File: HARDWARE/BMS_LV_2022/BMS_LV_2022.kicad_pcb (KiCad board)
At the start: 4 copper layers, 90 x 45 mm, 171 parts, among them J1 Conn_01x06_Male, J11 Conn_01x07_Female, J2 Conn_01x12_Male, J3 USB_B_Mini, J4 Battery+, J5 Battery-, J6 Conn_01x09_Female, Q1 BC846, Q10 BSS138, Q11 SiSS05DN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

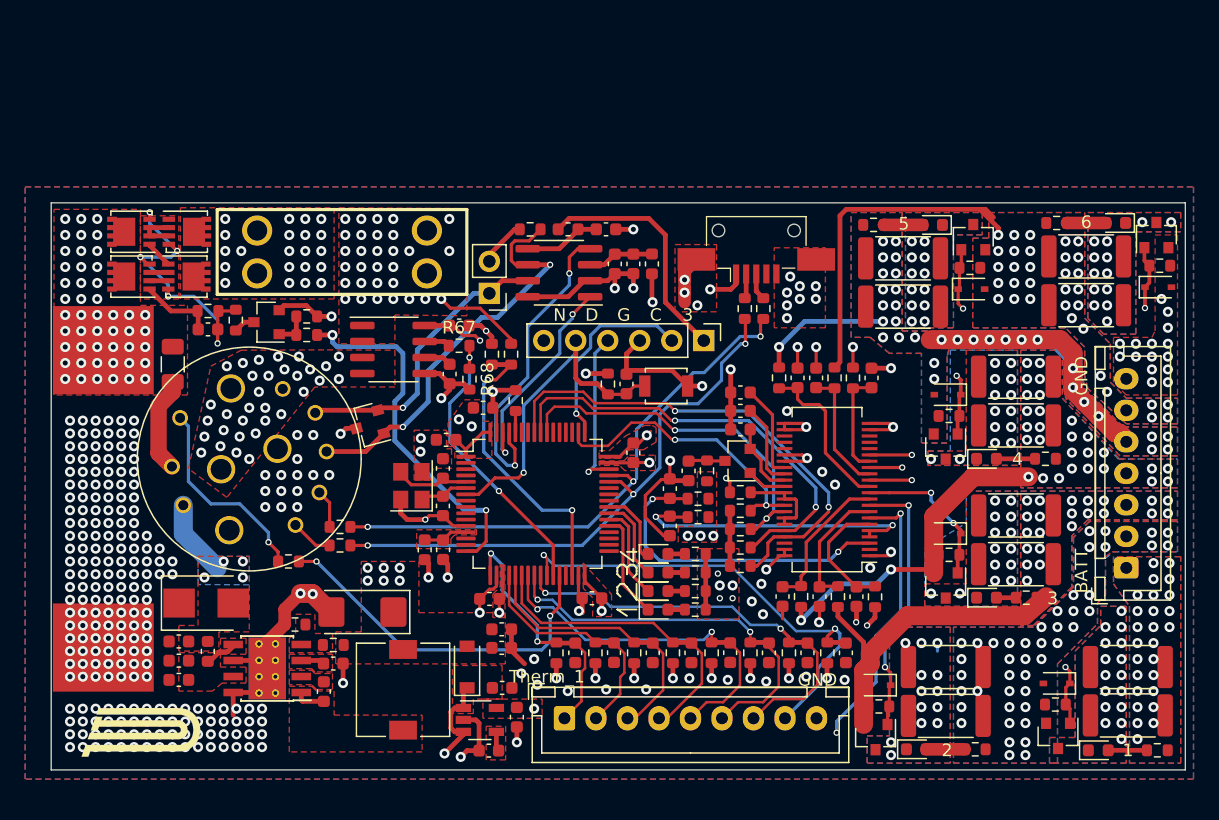
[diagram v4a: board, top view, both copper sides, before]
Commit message: New fuses and programming connector added
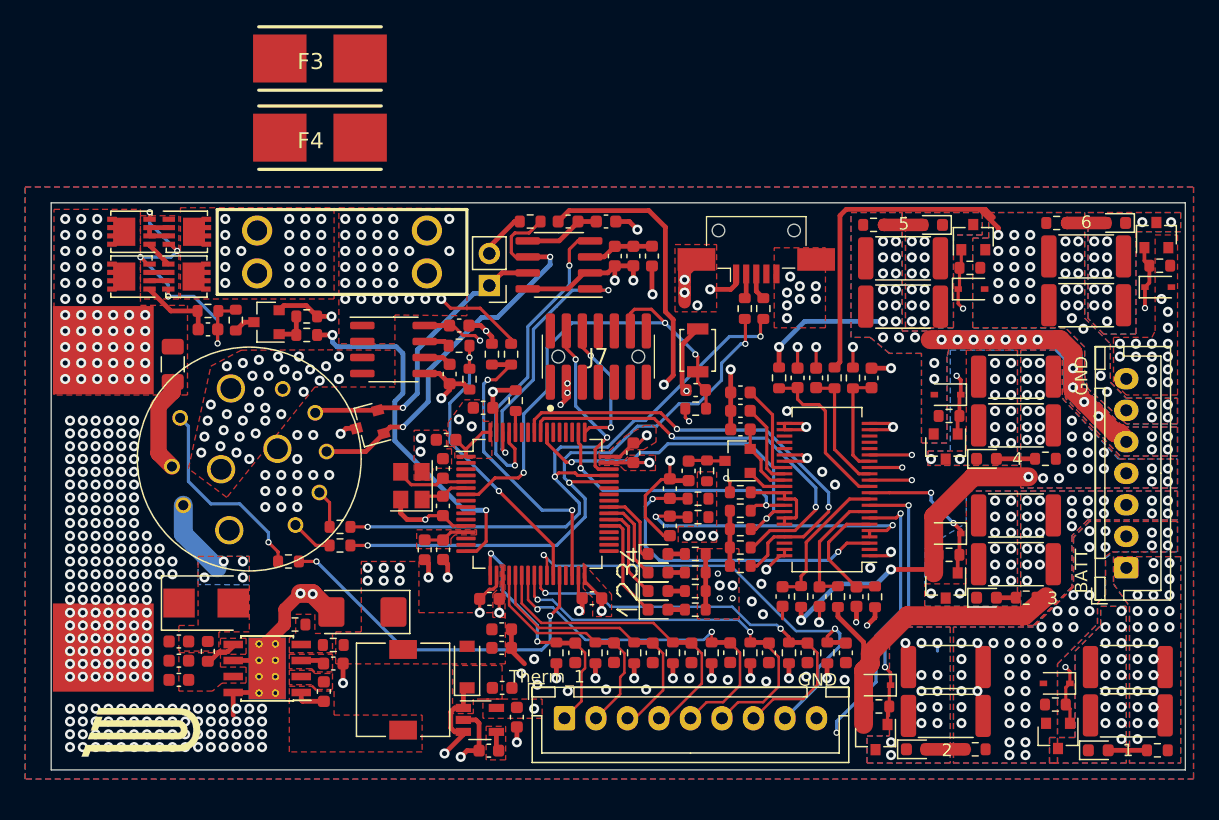
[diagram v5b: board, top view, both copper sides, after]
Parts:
- removed J1: Conn_01x06_Male, Connector_PinHeader_2.54mm:PinHeader_1x06_P2.54mm_Vertical
- added F3: Fuse, footprints:0154001.DRT, F.Cu at (131.3, 68.5)
- added F4: Fuse, footprints:0154001.DRT, F.Cu at (131.3, 74.8)
- added J7: FTSH, footprints:FTSH-107-XX-YYY-DV-K-A, F.Cu at (153.4, 92.2)
- moved R1 7.23 mm to (161.1, 96.3), turned to 180 degrees
- moved C1 5.51 mm to (161.1, 94.9), turned to 0 degrees
- moved SW1 3.78 mm to (161.3, 91.7), turned to 90 degrees
- moved JP2 0.62 mm to (144.8, 86.6)
- moved U4 0.62 mm to (150.3, 84.9)
- moved C7 0.62 mm to (156.2, 84.2)
- moved C8 0.62 mm to (154.7, 84.2)
- moved C9 0.62 mm to (154.0, 81.5)
- moved FB2 0.62 mm to (151.0, 81.5)
- moved FB3 0.62 mm to (157.7, 84.2)
- moved R4 0.62 mm to (148.0, 81.5)
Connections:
- F2 pad 2: Net-(F2-Pad2) -> Net-(Q11-D)
- J2 pad 1: Net-(J2-Pad1) -> unconnected-(J2-Pin_1-Pad1)
- J2 pad 10: /V_Out -> /V_Out_Pin_2
- J2 pad 9: /V_Out -> /V_Out_Pin_1
- J3 pad 4: Net-(J3-Pad4) -> unconnected-(J3-ID-Pad4)
- LTC68101 pad 18: Net-(LTC68101-Pad18) -> unconnected-(LTC68101-GPIO1-Pad18)
- LTC68101 pad 19: Net-(LTC68101-Pad19) -> unconnected-(LTC68101-GPIO2-Pad19)
- LTC68101 pad 2: Net-(LTC68101-Pad2) -> unconnected-(LTC68101-NC-Pad2)
- LTC68101 pad 20: Net-(LTC68101-Pad20) -> unconnected-(LTC68101-GPIO3-Pad20)
- LTC68101 pad 25: Net-(LTC68101-Pad25) -> unconnected-(LTC68101-GPIO4-Pad25)
- LTC68101 pad 26: Net-(LTC68101-Pad26) -> unconnected-(LTC68101-DTEN-Pad26)
- LTC68101 pad 27: Net-(LTC68101-Pad27) -> unconnected-(LTC68101-ISOMD-Pad27)
- LTC68101 pad 42: Net-(LTC68101-Pad42) -> unconnected-(LTC68101-WDT-Pad42)
- Q11 pad 5: Net-(F2-Pad2) -> /CS_IP+
- Q12 pad 5: Net-(F2-Pad2) -> /CS_IP+
- U1 pad 10: Net-(U1-Pad10) -> unconnected-(U1-PC2-Pad10)
- U1 pad 11: Net-(U1-Pad11) -> unconnected-(U1-PC3-Pad11)
- U1 pad 14: Net-(U1-Pad14) -> unconnected-(U1-PA0-Pad14)
- U1 pad 15: Net-(U1-Pad15) -> unconnected-(U1-PA1-Pad15)
- U1 pad 2: Net-(U1-Pad2) -> unconnected-(U1-PC13-Pad2)
- U1 pad 29: Net-(U1-Pad29) -> unconnected-(U1-PB10-Pad29)
- U1 pad 3: Net-(U1-Pad3) -> unconnected-(U1-PC14-OSC32_IN-Pad3)
- U1 pad 33: Net-(U1-Pad33) -> unconnected-(U1-PB12-Pad33)
- U1 pad 34: Net-(U1-Pad34) -> unconnected-(U1-PB13-Pad34)
- U1 pad 35: Net-(U1-Pad35) -> unconnected-(U1-PB14-Pad35)
- U1 pad 36: Net-(U1-Pad36) -> unconnected-(U1-PB15-Pad36)
- U1 pad 4: Net-(U1-Pad4) -> unconnected-(U1-PC15-OSC32_OUT-Pad4)
- U1 pad 41: Net-(U1-Pad41) -> unconnected-(U1-PA8-Pad41)
- U1 pad 42: Net-(U1-Pad42) -> unconnected-(U1-PA9-Pad42)
- U1 pad 43: Net-(U1-Pad43) -> unconnected-(U1-PA10-Pad43)
- U1 pad 51: Net-(U1-Pad51) -> unconnected-(U1-PC10-Pad51)
- U1 pad 52: Net-(U1-Pad52) -> unconnected-(U1-PC11-Pad52)
- U1 pad 53: Net-(U1-Pad53) -> unconnected-(U1-PC12-Pad53)
- U1 pad 54: Net-(U1-Pad54) -> unconnected-(U1-PD2-Pad54)
- U1 pad 58: Net-(U1-Pad58) -> unconnected-(U1-PB6-Pad58)
- U1 pad 59: Net-(U1-Pad59) -> unconnected-(U1-PB7-Pad59)
- U1 pad 8: Net-(U1-Pad8) -> unconnected-(U1-PC0-Pad8)
- U1 pad 9: Net-(U1-Pad9) -> unconnected-(U1-PC1-Pad9)
- U5 pad 3: /V_Out -> Net-(F3-Pad1)
- U5 pad 4: /V_Out -> Net-(F3-Pad1)
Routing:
- net /NRST: track 26.8 -> 39.0 mm, vias 1 -> 3
- net /USB-DP: track 44.7 -> 50.4 mm
- net /SW-CLK: track 15.7 -> 10.8 mm, vias 1 -> 2
- net +3V3: track 56.3 -> 60.6 mm, vias 21 -> 25
- net /CAN-TX: track 17.1 -> 21.3 mm
- net /USB-DM: track 45.6 -> 49.0 mm
- net GND: track 134.2 -> 131.1 mm
- net /MOSI: track 39.5 -> 37.3 mm
- net /MISO: track 35.3 -> 33.2 mm
- net /SW-DIO: track 12.8 -> 13.7 mm, vias 1 -> 2
- net /SCK: track 29.2 -> 28.4 mm
- net /CS: track 22.9 -> 22.1 mm
- net /CAN-RX: track 24.7 -> 25.3 mm
- net /CANL: track 32.6 -> 33.2 mm
- net Net-(F3-Pad1): vias 0 -> 32
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- added copper zone on In1.Cu, net /V_Out_Pin_2
- added copper zone on F.Cu, net Net-(F3-Pad1)
- removed copper zone on F.Cu, net /V_Out
- removed copper zone on In1.Cu, net /V_Out
- removed copper zone on F.Cu, net Net-(F2-Pad2)
- removed copper zone on In1.Cu, net Net-(F2-Pad2)
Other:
- board text removed: "C"
- board text removed: "D"
- board text removed: "G"
- board text removed: "N"

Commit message: Significant changes
-main connector changed to the other side of the pcb because of using socket connector in the new version
-changed usb mini to usb-c
-changed fuse to 2 fuses protecting current path pins separately
-some minor changes in layout
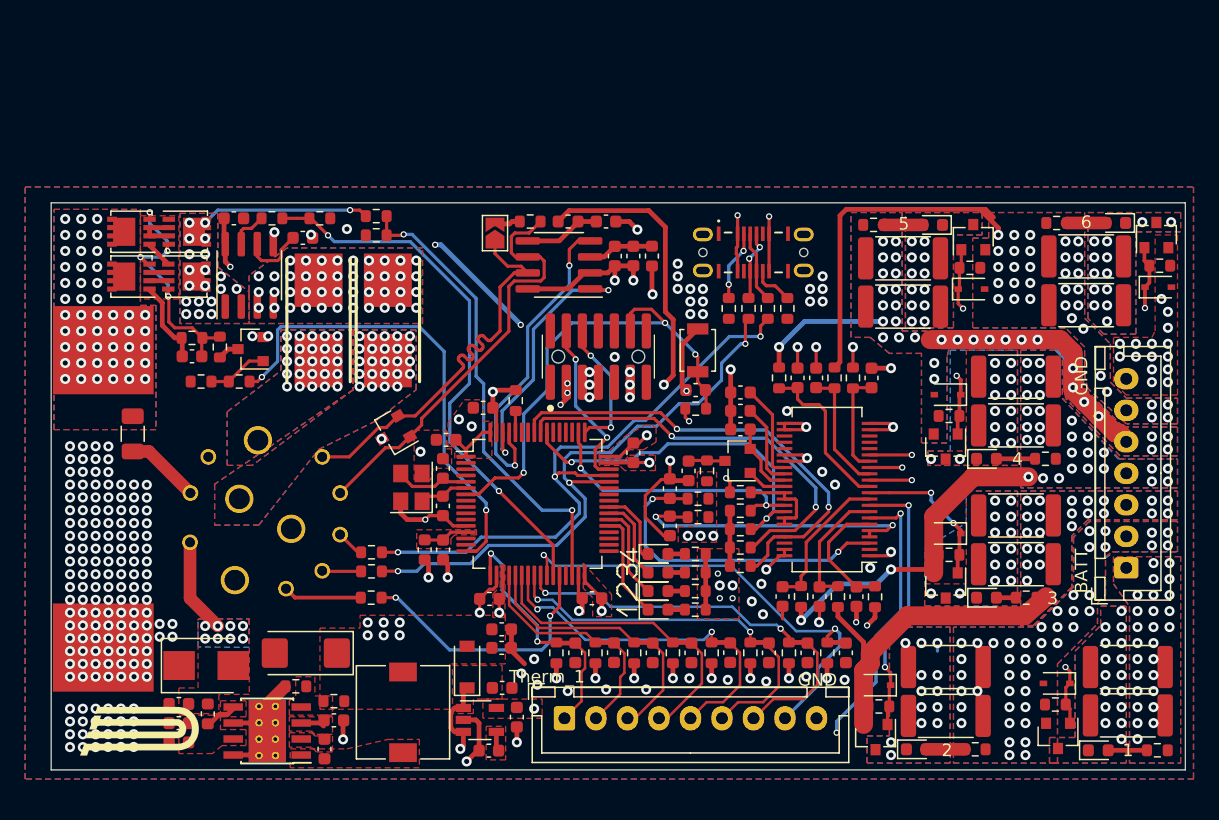
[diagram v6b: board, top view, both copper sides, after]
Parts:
- removed F2: Fuse, footprints:3557-2
- removed J3: USB_B_Mini, Connector_USB:USB_Mini-B_AdamTech_MUSB-B5-S-VT-TSMT-1_SMD_Vertical
- added J1: USB-C_GCT_USB4145-03-0070-C, footprints:USB-C_Receptacle_GCT_USB4145-03-0070-C, F.Cu at (165.7, 83.8)
- added R69: 5.1k, Resistor_SMD:R_0603_1608Metric, F.Cu at (163.8, 88.4)
- added R70: 5.1k, Resistor_SMD:R_0603_1608Metric, F.Cu at (168.4, 88.4)
- J2: moved to B.Cu
- JP2: footprint Connector_PinHeader_2.54mm:PinHeader_1x02_P2.54mm_Vertical -> Jumper:SolderJumper-2_P1.3mm_Open_TrianglePad1.0x1.5mm
- R66: value 2,7k -> 2.7k
- moved F3 21.5 mm to (136.7, 89.3), turned to -90 degrees
- moved C43 19.8 mm to (124.5, 81.2)
- moved R67 18.0 mm to (127.5, 81.2)
- moved R68 17.4 mm to (131.3, 81.2), turned to 0 degrees
- moved C42 15.9 mm to (130.0, 82.8), turned to 0 degrees
- moved R65 15.3 mm to (135.8, 81.1), turned to 0 degrees
- moved F4 14.5 mm to (131.2, 89.3), turned to -90 degrees
- moved R66 13.2 mm to (135.8, 82.6), turned to 180 degrees
- moved U5 12.9 mm to (125.7, 85.8), turned to 90 degrees
- moved R60 9.85 mm to (121.9, 94.2), turned to 180 degrees
- moved R15 7.16 mm to (135.4, 111.3)
- moved R59 6.51 mm to (124.9, 94.2)
- moved F1 6.37 mm to (116.5, 98.3)
- moved C38 5.55 mm to (130.2, 115.7)
- moved C32 4.96 mm to (120.1, 121.3)
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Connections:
- D2 pad 1: /CANL -> /CAN-
- D2 pad 2: /CANH -> /CAN+
- J2 pad 1: unconnected-(J2-Pin_1-Pad1) -> Net-(J2-Pin_1)
- J2 pad 10: /V_Out_Pin_2 -> /V_Out_Pin_1
- J2 pad 12: GND -> /V_Out_Pin_2
- J2 pad 2: /CANH -> Net-(J2-Pin_2)
- J2 pad 3: /CANL -> Net-(J2-Pin_3)
- J2 pad 4: Net-(J2-Pin_4) -> /CAN-
- J2 pad 5: Net-(J2-Pin_5) -> /CAN+
- J2 pad 6: VCC -> unconnected-(J2-Pin_6-Pad6)
- J2 pad 8: Net-(J2-Pin_8) -> VCC
- J2 pad 9: /V_Out_Pin_1 -> GND
- JP2 pad 1: /CANH -> /CAN+
- R13 pad 2: Net-(J2-Pin_4) -> Net-(J2-Pin_3)
- R14 pad 1: Net-(J2-Pin_5) -> Net-(J2-Pin_2)
- R15 pad 1: Net-(J2-Pin_8) -> Net-(J2-Pin_1)
- R4 pad 2: /CANL -> /CAN-
- R8 pad 1: Net-(J3-D+) -> /D+
- R9 pad 2: Net-(J3-D-) -> /D-
- U4 pad 6: /CANL -> /CAN-
- U4 pad 7: /CANH -> /CAN+
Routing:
- net /CAN-: track 0.00 -> 34.0 mm
- net /CANL: track 33.2 -> 0.00 mm, vias 2 -> 0
- net /CAN+: track 0.00 -> 32.4 mm
- net +5V: track 45.7 -> 71.7 mm, vias 8 -> 10
- net GND: track 131.1 -> 105.3 mm, vias 300 -> 240
- net /CANH: track 23.2 -> 0.00 mm, vias 1 -> 0
- net /CurrentSensor_Out: track 23.2 -> 43.4 mm
- net Net-(J2-Pin_8): track 15.9 -> 0.00 mm, vias 1 -> 0
- net /VoltageFuseMeasure: track 23.8 -> 37.3 mm
- net /Switch_Signal: track 28.9 -> 37.9 mm
- net /Interlock: track 28.7 -> 20.9 mm
- net Net-(J2-Pin_1): track 0.00 -> 6.22 mm
- net /CS_IP+: track 7.23 -> 13.4 mm, vias 51 -> 20
- net /D-: track 0.00 -> 5.80 mm, vias 0 -> 2
- net /D+: track 0.00 -> 5.74 mm
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- added copper zone on B.Cu, net +24V
- added copper zone on In2.Cu, net +24V
- added copper zone on B.Cu, net /CS_IP+
- added copper zone on In2.Cu, net /CS_IP+
- added copper zone on B.Cu, net /V_Out_Pin_1
- added copper zone on F.Cu, net /V_Out_Pin_1
- added copper zone on In1.Cu, net /V_Out_Pin_1
- added copper zone on In2.Cu, net /V_Out_Pin_1
- added copper zone on B.Cu, net /V_Out_Pin_2
- added copper zone on F.Cu, net /V_Out_Pin_2
- added copper zone on In2.Cu, net /V_Out_Pin_2
- added copper zone on B.Cu, net Net-(F3-Pad1)
- added copper zone on In1.Cu, net Net-(F3-Pad1)
- added copper zone on In2.Cu, net Net-(F3-Pad1)
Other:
- board text added: "2024"
- board text added: "V2.0"
- board text removed: "2022"
- board text removed: "V1.0"

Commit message: Version 2.0
Grounding corrected and production files added
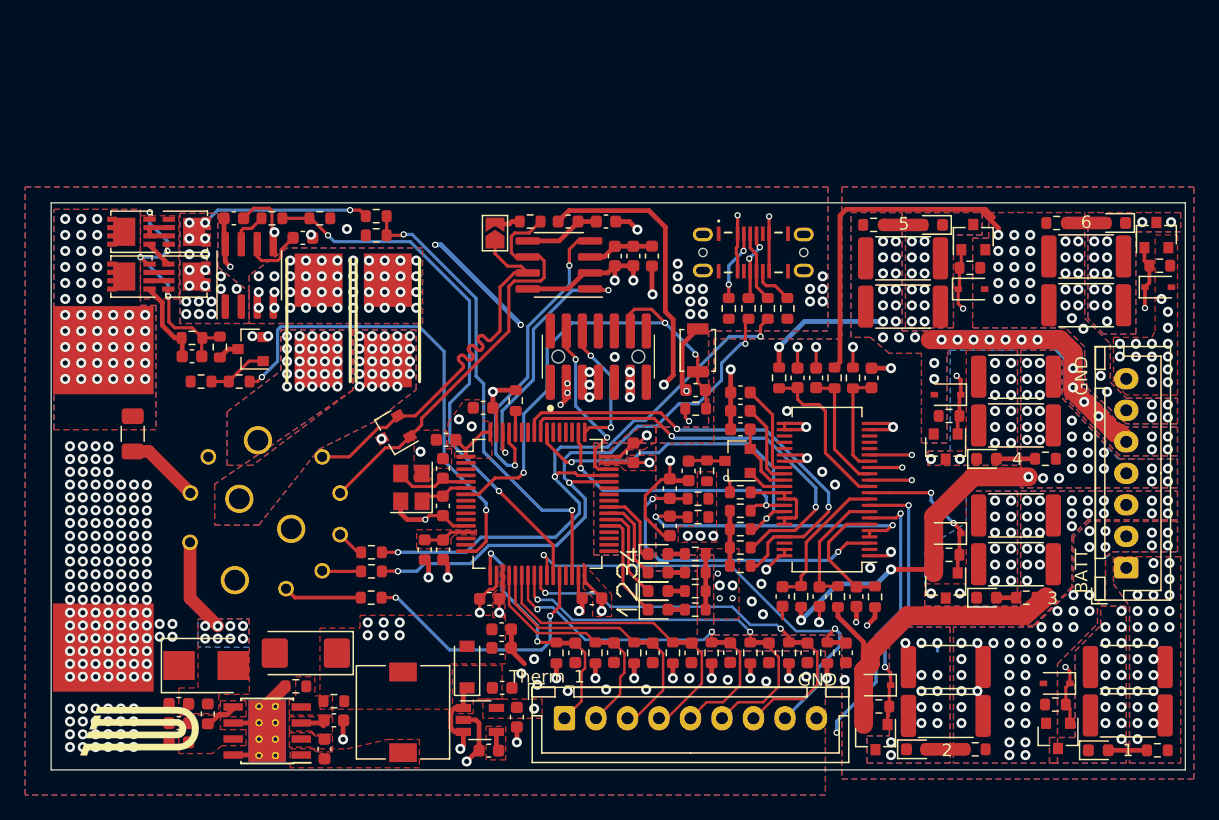
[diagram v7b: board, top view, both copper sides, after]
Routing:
- net GND: track 105.3 -> 109.7 mm
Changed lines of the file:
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@@
 		(tags "capacitor")
 		(property "Reference" "C42"
-			(at 0 -1.43 360)
+			(at 0 -1.43 0)
 			(layer "F.SilkS")
 			(hide yes)
@@
 		)
 		(property "Value" "1nF"
-			(at 0 1.43 360)
+			(at 0 1.43 0)
 			(layer "F.Fab")
 			(effects
@@
 		)
 		(fp_text user "${REFERENCE}"
-			(at 0 0 360)
+			(at 0 0 0)
 			(layer "F.SilkS")
 			(hide yes)
@@
 		(tags "solder jumper open")
 		(property "Reference" "JP2"
-			(at 0 -1.8 270)
+			(at 0 -1.8 -90)
 			(layer "F.SilkS")
 			(hide yes)
@@
 		)
 		(property "Value" "CAN_terminanion_jumper"
-			(at 0 1.9 270)
+			(at 0 1.9 -90)
 			(layer "F.Fab")
 			(effects
@@
 		(tags "resistor")
 		(property "Reference" "R59"
-			(at 0 -1.43 360)
+			(at 0 -1.43 0)
 			(layer "F.SilkS")
 			(hide yes)
@@
 		)
 		(property "Value" "100"
-			(at 0 1.43 360)
+			(at 0 1.43 0)
 			(layer "F.Fab")
 			(effects
@@
 		)
 		(fp_text user "${REFERENCE}"
-			(at 0 0 360)
+			(at 0 0 0)
 			(layer "F.SilkS")
 			(hide yes)
@@
 		(tags "SOIC SO")
 		(property "Reference" "U5"
-			(at 0 -3.4 270)
+			(at 0 -3.4 -90)
 			(layer "F.SilkS")
 			(hide yes)
@@
 		)
 		(property "Value" "ACHS-7123"
-			(at 0 3.4 270)
+			(at 0 3.4 -90)
 			(layer "F.Fab")
 			(effects
@@
 		)
 		(fp_text user "${REFERENCE}"
-			(at 0 0 270)
+			(at 0 0 -90)
 			(layer "F.SilkS")
 			(hide yes)
@@
 		(tags "resistor")
 		(property "Reference" "R65"
-			(at 0 -1.43 360)
+			(at 0 -1.43 0)
 			(layer "F.SilkS")
 			(hide yes)
@@
 		)
 		(property "Value" "20k"
-			(at 0 1.43 360)
+			(at 0 1.43 0)
 			(layer "F.Fab")
 			(effects
@@
 		)
 		(fp_text user "${REFERENCE}"
-			(at 0 0 360)
+			(at 0 0 0)
 			(layer "F.SilkS")
 			(hide yes)
@@
 		(tags "resistor")
 		(property "Reference" "R68"
-			(at 0 -1.43 360)
+			(at 0 -1.43 0)
 			(layer "F.SilkS")
 			(hide yes)
@@
 		)
 		(property "Value" "2k"
-			(at 0 1.43 360)
+			(at 0 1.43 0)
 			(layer "F.Fab")
 			(effects
@@
 		)
 		(fp_text user "${REFERENCE}"
-			(at 0 0 360)
+			(at 0 0 0)
 			(layer "F.Fab")
 			(effects
@@
 				(font
 					(size 1.27 1.27)
+					(thickness 0.15)
 				)
 			)
@@
 				(font
 					(size 1.27 1.27)
+					(thickness 0.15)
 				)
 			)
@@
 				(font
 					(size 1.27 1.27)
+					(thickness 0.15)
 				)
 			)
@@
 		(at 126.987903 104.68 90)
 		(property "Reference" "J2"
-			(at -0.000001 10.16 270)
+			(at -0.000001 10.16 -90)
 			(layer "B.SilkS")
 			(hide yes)
@@
 		)
 		(property "Value" "Conn_01x12_Male"
-			(at 0 11.93 270)
+			(at 0 11.93 -90)
 			(layer "B.Fab")
 			(effects
@@
 	)
 	(segment
+		(start 126.067903 80.43)
+		(end 127.315907 80.43)
+		(width 0.25)
+		(layer "F.Cu")
+		(net 2)
+	)
+	(segment
 		(start 137.733903 104.627)
 		(end 137.733903 103.68)
@@
 	)
 	(segment
+		(start 127.517903 82.13)
+		(end 127.717903 82.33)
+		(width 0.25)
+		(layer "F.Cu")
+		(net 2)
+	)
+	(segment
 		(start 163.919503 95.0468)
 		(end 163.919503 93.218)
@@
 	)
 	(segment
+		(start 127.315907 80.43)
+		(end 127.517903 80.631996)
+		(width 0.25)
+		(layer "F.Cu")
+		(net 2)
+	)
+	(segment
 		(start 168.034303 112.0146)
 		(end 168.034303 113.0046)
@@
 	)
 	(segment
+		(start 127.517903 80.631996)
+		(end 127.517903 82.13)
+		(width 0.25)
+		(layer "F.Cu")
+		(net 2)
+	)
+	(segment
 		(start 154.724703 85.000897)
 		(end 154.724703 86.2458)
@@
 	)
 	(segment
+		(start 125.267903 81.23)
+		(end 126.067903 80.43)
+		(width 0.25)
+		(layer "F.Cu")
+		(net 2)
+	)
+	(segment
 		(start 146.8628 94.87)
 		(end 145.173903 94.87)
@@
 	)
 	(segment
-		(start 125.890903 82.032)
-		(end 126.692903 81.23)
+		(start 125.082903 82.215)
+		(end 125.265903 82.032)
 		(width 0.254)
 		(layer "F.Cu")
@@
 	)
 	(segment
-		(start 125.082903 82.215)
-		(end 125.265903 82.032)
+		(start 125.890903 82.032)
+		(end 126.692903 81.23)
 		(width 0.254)
 		(layer "F.Cu")
@@
 		(layers "F.Cu" "In2.Cu" "B.Cu")
 		(hatch edge 0.508)
+		(priority 1)
 		(connect_pads yes
-			(clearance 0.408)
+			(clearance 0.508)
+		)
+		(min_thickness 0.254)
+		(filled_areas_thickness no)
+		(fill yes
+			(thermal_gap 0.508)
+			(thermal_bridge_width 0.508)
+		)
+		(polygon
+			(pts
+				(xy 200.673303 125.73) (xy 200.673303 78.74) (xy 172.733303 78.74) (xy 172.733303 90.805) (xy 162.573303 90.805)
+				(xy 162.573303 99.06) (xy 153.048303 99.06) (xy 153.048303 107.95) (xy 162.573303 107.95) (xy 162.573303 113.03)
+				(xy 162.573303 114.3) (xy 172.733303 114.3) (xy 172.733303 125.73)
+			)
+		)
+	)
+	(zone
+		(net 2)
+		(net_name "GND")
+		(layers "F.Cu" "In2.Cu" "B.Cu")
+		(hatch edge 0.508)
+		(connect_pads yes
+			(clearance 0.508)
 		)
 		(min_thickness 0.254)
@@
 		(polygon
 			(pts
-				(xy 200.647903 125.73) (xy 107.937903 125.73) (xy 107.937903 78.74) (xy 200.647903 78.74)
+				(xy 171.637903 78.74) (xy 171.637903 90.17) (xy 162.166903 90.17) (xy 162.166903 97.79) (xy 157.975903 97.79)
+				(xy 157.975903 109.22) (xy 161.277903 109.22) (xy 161.277903 115.57) (xy 171.437903 115.57) (xy 171.437903 127)
+				(xy 107.937903 127) (xy 107.937903 78.74)
 			)
 		)
@@
 			)
 		)
-	)
-	(zone
-		(net 2)
-		(net_name "GND")
-		(layer "In2.Cu")
-		(hatch edge 0.508)
-		(priority 1)
-		(connect_pads
-			(clearance 0.508)
-		)
-		(min_thickness 0.254)
-		(filled_areas_thickness no)
-		(fill yes
-			(thermal_gap 0.508)
-			(thermal_bridge_width 0.508)
-		)
-		(polygon
-			(pts
-				(xy 200.673303 125.73) (xy 200.673303 78.74) (xy 172.733303 78.74) (xy 172.733303 90.805) (xy 162.573303 90.805)
-				(xy 162.573303 99.06) (xy 153.048303 99.06) (xy 153.048303 107.95) (xy 162.573303 107.95) (xy 162.573303 113.03)
-				(xy 162.573303 114.3) (xy 172.733303 114.3) (xy 172.733303 125.73)
-			)
-		)

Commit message: Autosport connector scheme updated
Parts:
- J2: value Conn_01x12_Male -> AS214-97PN
- moved J2 0.10 mm to (127.0, 104.6)
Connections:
- R13 pad 2: Net-(J2-Pin_3) -> Net-(J2-PadK)
- R14 pad 1: Net-(J2-Pin_2) -> Net-(J2-PadJ)
- R15 pad 1: Net-(J2-Pin_1) -> Net-(J2-PadH)
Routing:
- net Net-(J2-Pin_1): track 6.22 -> 0.00 mm
- net Net-(J2-PadH): track 0.00 -> 6.22 mm
- net Net-(J2-Pin_2): track 3.10 -> 0.00 mm
- net Net-(J2-PadJ): track 0.00 -> 3.10 mm
- net Net-(J2-Pin_3): track 2.24 -> 0.00 mm
- net Net-(J2-PadK): track 0.00 -> 2.24 mm
